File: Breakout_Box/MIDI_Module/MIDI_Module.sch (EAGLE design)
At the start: 82 parts, among them Q1 QUARZ5, T1 2N2222, T2 2N2222, U1 LMV324, U2 LMV324, U3 MIC5205-5.0YM5-TR, U4 MIC5205-3.3, U5 MSP430G2553RHB32

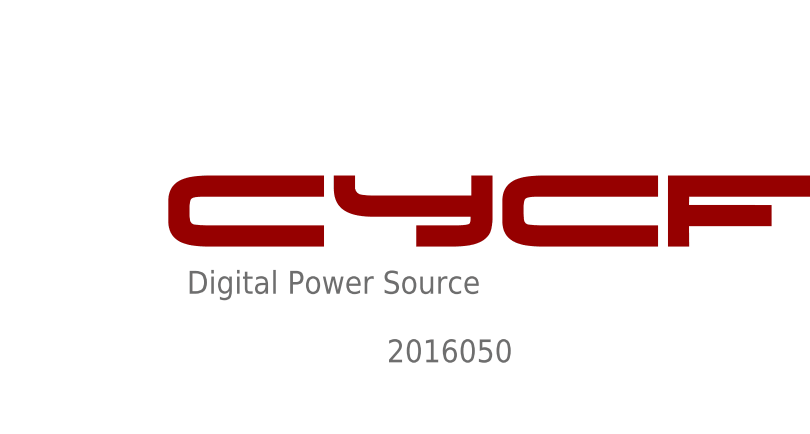
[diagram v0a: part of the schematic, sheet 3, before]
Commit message: Update page title name
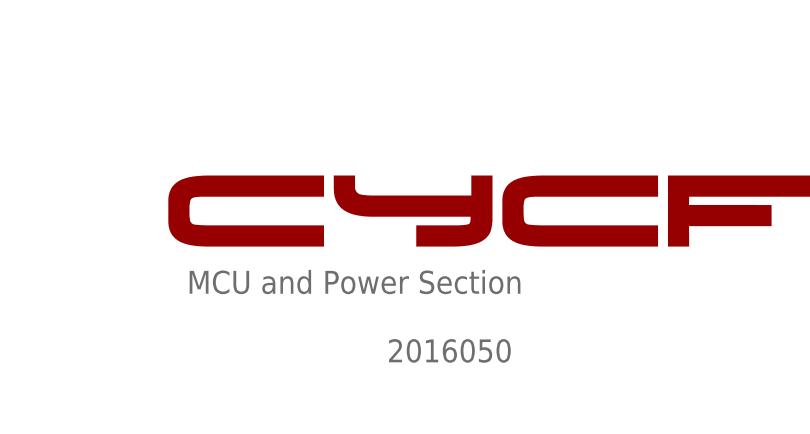
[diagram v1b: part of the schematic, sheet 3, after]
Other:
- note added: "MCU and Power Section"
- note removed: "Digital Power Source"
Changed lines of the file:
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@@
 <setting verticaltext="up"/>
 </settings>
-<grid distance="0.025" unitdist="inch" unit="inch" style="lines" multiple="1" display="yes" altdistance="0.01" altunitdist="inch" altunit="inch"/>
+<grid distance="0.1" unitdist="inch" unit="inch" style="lines" multiple="1" display="no" altdistance="0.01" altunitdist="inch" altunit="inch"/>
 <layers>
 <layer number="1" name="Top" color="4" fill="1" visible="no" active="no"/>
@@
 <sheet>
 <plain>
-<text x="177.8" y="19.05" size="2.54" layer="95">Digital Power Source</text>
+<text x="177.8" y="19.05" size="2.54" layer="95">MCU and Power Section</text>
 <text x="12.7" y="34.925" size="1.778" layer="95">NOTES:
 *MCU_VCC = 5V MCU power supply
